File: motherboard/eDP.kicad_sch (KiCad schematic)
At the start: 4 parts, among them J2 20455-040E-76 OLED IPEX, J6 OLED EL POWER

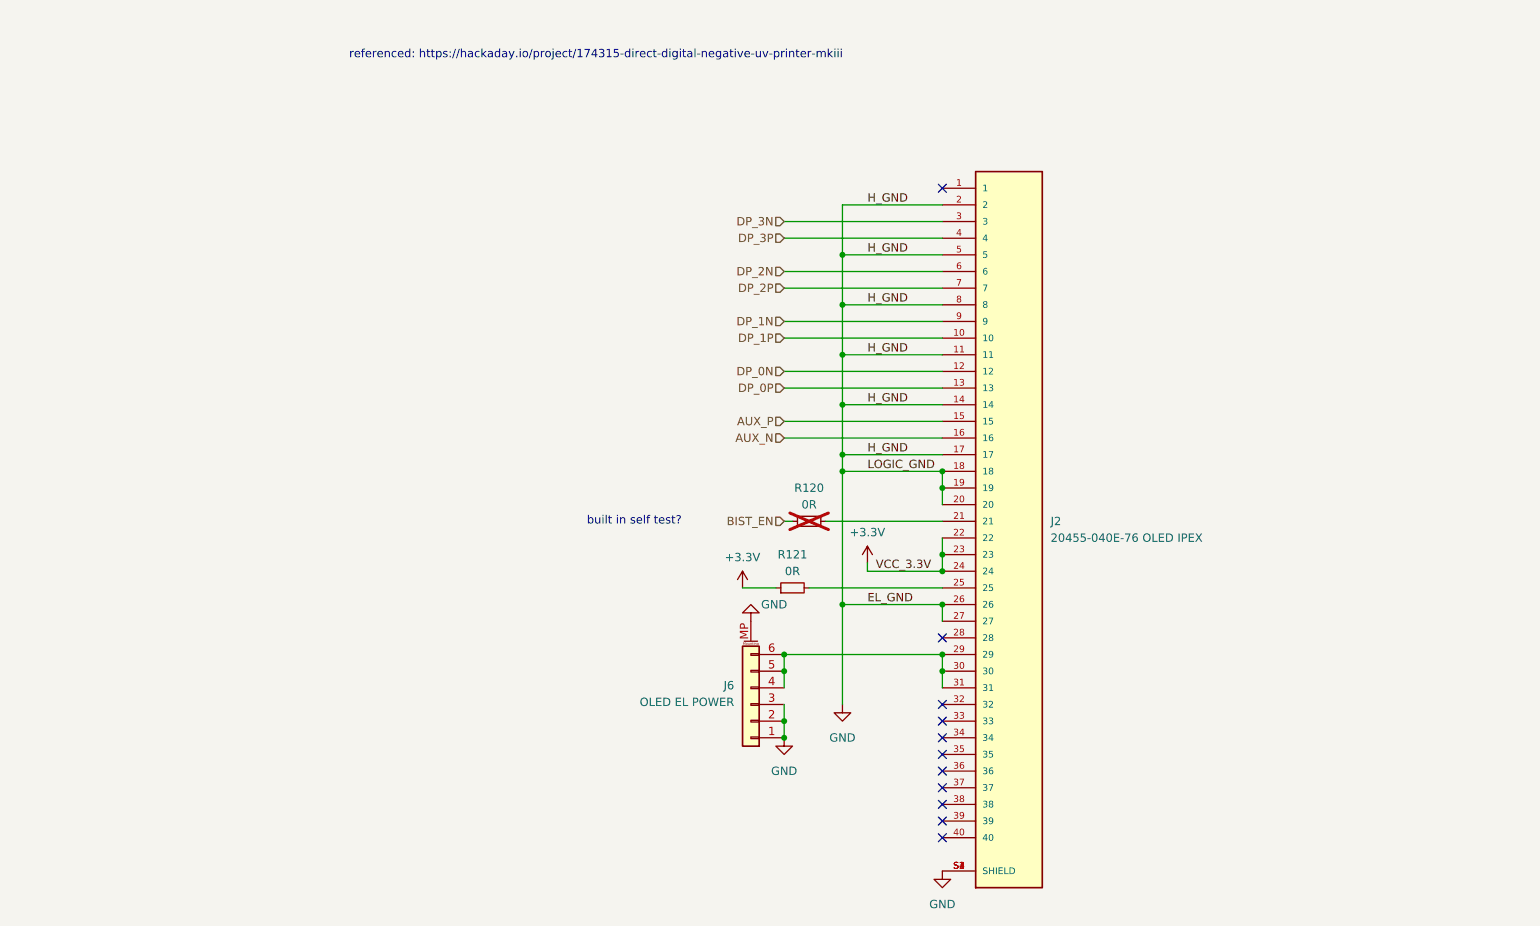
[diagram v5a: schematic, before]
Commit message: created display evaluation board + layout modifications
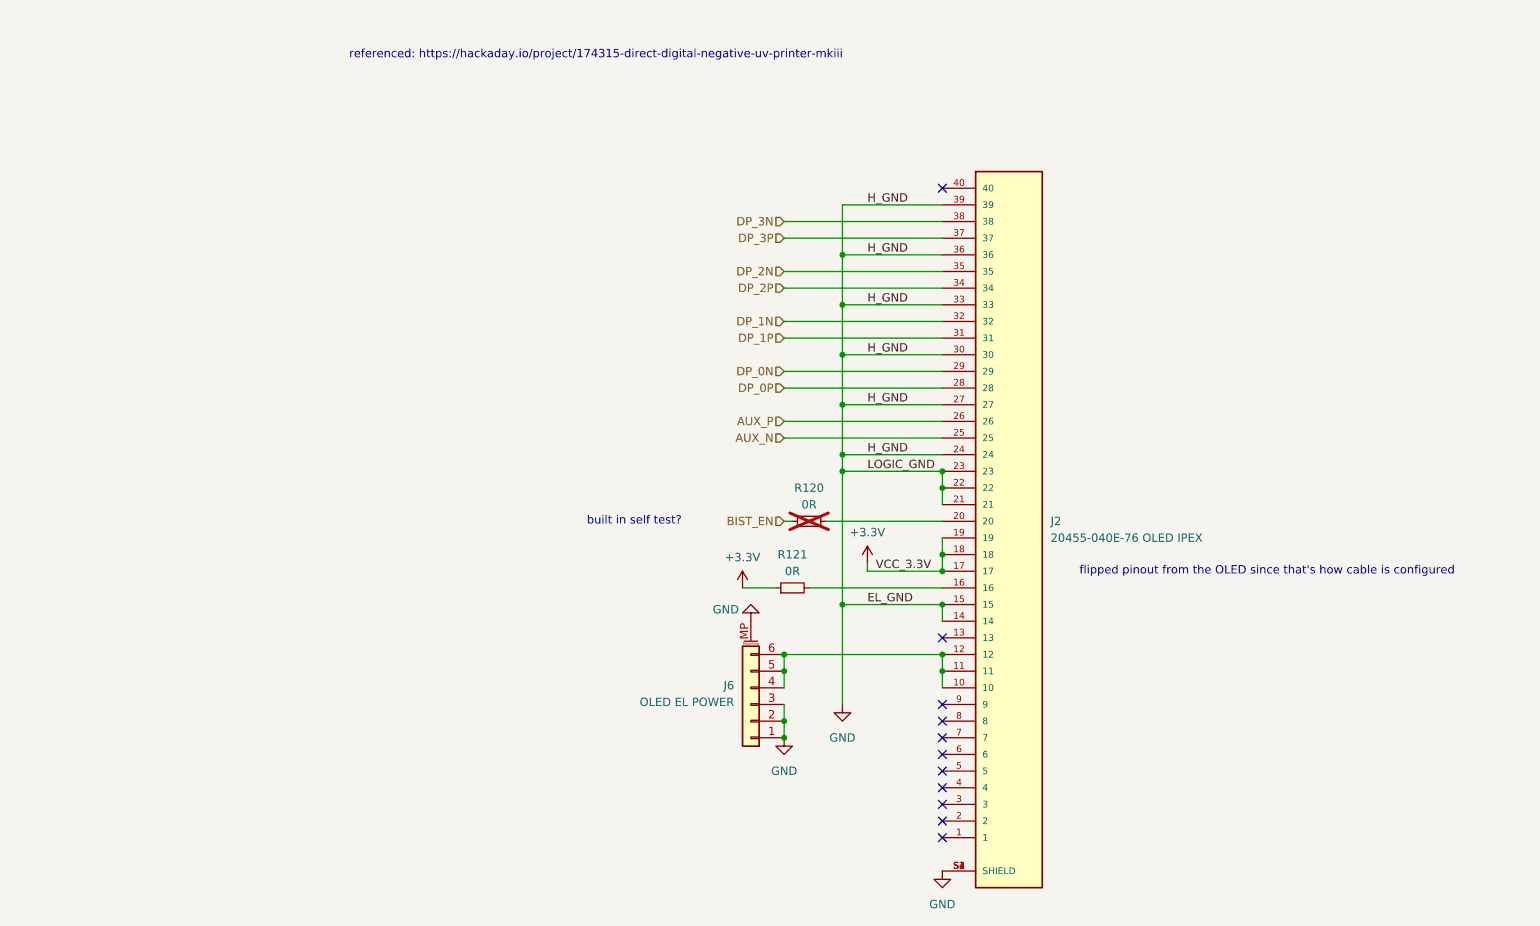
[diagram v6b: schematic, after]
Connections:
- net +3.3V: now also J2.17, J2.18, J2.19; no longer J2.22, J2.23, J2.24
- net AUX_N: now also J2.25; no longer J2.16
- net AUX_P: now also J2.26; no longer J2.15
- net DP_0N: now also J2.29; no longer J2.12
- net DP_0P: now also J2.28; no longer J2.13
- net DP_1N: now also J2.32; no longer J2.9
- net DP_1P: now also J2.31; no longer J2.10
- net DP_2N: now also J2.35; no longer J2.6
- net DP_2P: now also J2.34; no longer J2.7
- net DP_3N: now also J2.38; no longer J2.3
- net DP_3P: now also J2.37; no longer J2.4
- net GND: now also J2.15, J2.21, J2.22, J2.23, J2.24, J2.30, J2.33, J2.36, J2.39; no longer J2.11, J2.17, J2.18, J2.19, J2.2, J2.20, J2.26, J2.5, J2.8
- net at R121.2: now also J2.16; no longer J2.25
- net at R120.2: now also J2.20; no longer J2.21
- net at J6.4 (Pin_4), J6.5 (Pin_5), J6.6 (Pin_6): now also J2.10, J2.11, J2.12; no longer J2.29, J2.30, J2.31
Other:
- note added: "flipped pinout from the OLED since that's how cable is configured"
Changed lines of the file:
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@@
 		(comment 4 "Proof of concept board for feature verification")
+	)
+	(text "flipped pinout from the OLED since that's how cable is configured"
+		(exclude_from_sim no)
+		(at 203.2 107.95 0)
+		(effects
+			(font
+				(size 1.27 1.27)
+			)
+		)
 	)
 	(text "referenced: https://hackaday.io/project/174315-direct-digital-negative-uv-printer-mkiii"
@@
 			)
 			(justify right)
+		)
+	)
+	(symbol
+		(lib_id "power:GND")
+		(at 124.46 115.57 180)
+		(unit 1)
+		(exclude_from_sim no)
+		(in_bom yes)
+		(on_board yes)
+		(dnp no)
+		(property "Reference" "#PWR064"
+			(at 124.46 109.22 0)
+			(effects
+				(font
+					(size 1.27 1.27)
+				)
+				(hide yes)
+			)
+		)
+		(property "Value" "GND"
+			(at 120.65 113.792 0)
+			(effects
+				(font
+					(size 1.27 1.27)
+				)
+			)
+		)
+		(property "Footprint" ""
+			(at 124.46 115.57 0)
+			(effects
+				(font
+					(size 1.27 1.27)
+				)
+				(hide yes)
+			)
+		)
+		(property "Datasheet" ""
+			(at 124.46 115.57 0)
+			(effects
+				(font
+					(size 1.27 1.27)
+				)
+				(hide yes)
+			)
+		)
+		(property "Description" "Power symbol creates a global label with name \"GND\" , ground"
+			(at 124.46 115.57 0)
+			(effects
+				(font
+					(size 1.27 1.27)
+				)
+				(hide yes)
+			)
+		)
+		(pin "1"
+		)
+		(instances
+			(project "motherboard"
+				(path "/025fe4d1-0305-4b34-be04-f8d9818125a4/41516588-89d4-4c4a-8d7d-a4354a401e31"
+					(reference "#PWR064")
+					(unit 1)
+				)
+			)
 		)
 	)
@@
 					(unit 1)
 				)
-			)
-		)
-	)
-	(symbol
-		(lib_id "eDP_adaptor_board-rescue:GND-power")
-		(at 124.46 115.57 0)
-		(mirror x)
-		(unit 1)
-		(exclude_from_sim no)
-		(in_bom yes)
-		(on_board yes)
-		(dnp no)
-		(property "Reference" "#PWR0161"
-			(at 124.46 109.22 0)
-			(effects
-				(font
-					(size 1.27 1.27)
-				)
-				(hide yes)
-			)
-		)
-		(property "Value" "GND"
-			(at 128.016 113.03 0)
-			(effects
-				(font
-					(size 1.27 1.27)
-				)
-			)
-		)
-		(property "Footprint" ""
-			(at 124.46 115.57 0)
-			(effects
-				(font
-					(size 1.27 1.27)
-				)
-				(hide yes)
-			)
-		)
-		(property "Datasheet" ""
-			(at 124.46 115.57 0)
-			(effects
-				(font
-					(size 1.27 1.27)
-				)
-				(hide yes)
-			)
-		)
-		(property "Description" ""
-			(at 124.46 115.57 0)
-			(effects
-				(font
-					(size 1.27 1.27)
-				)
-			)
-		)
-		(pin "1"
-		)
-		(instances
-			(project "motherboard"
-				(path "/025fe4d1-0305-4b34-be04-f8d9818125a4/41516588-89d4-4c4a-8d7d-a4354a401e31"
-					(reference "#PWR0161")
-					(unit 1)
-				)

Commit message: starting motherboard v0.2
lessons from display eval v1
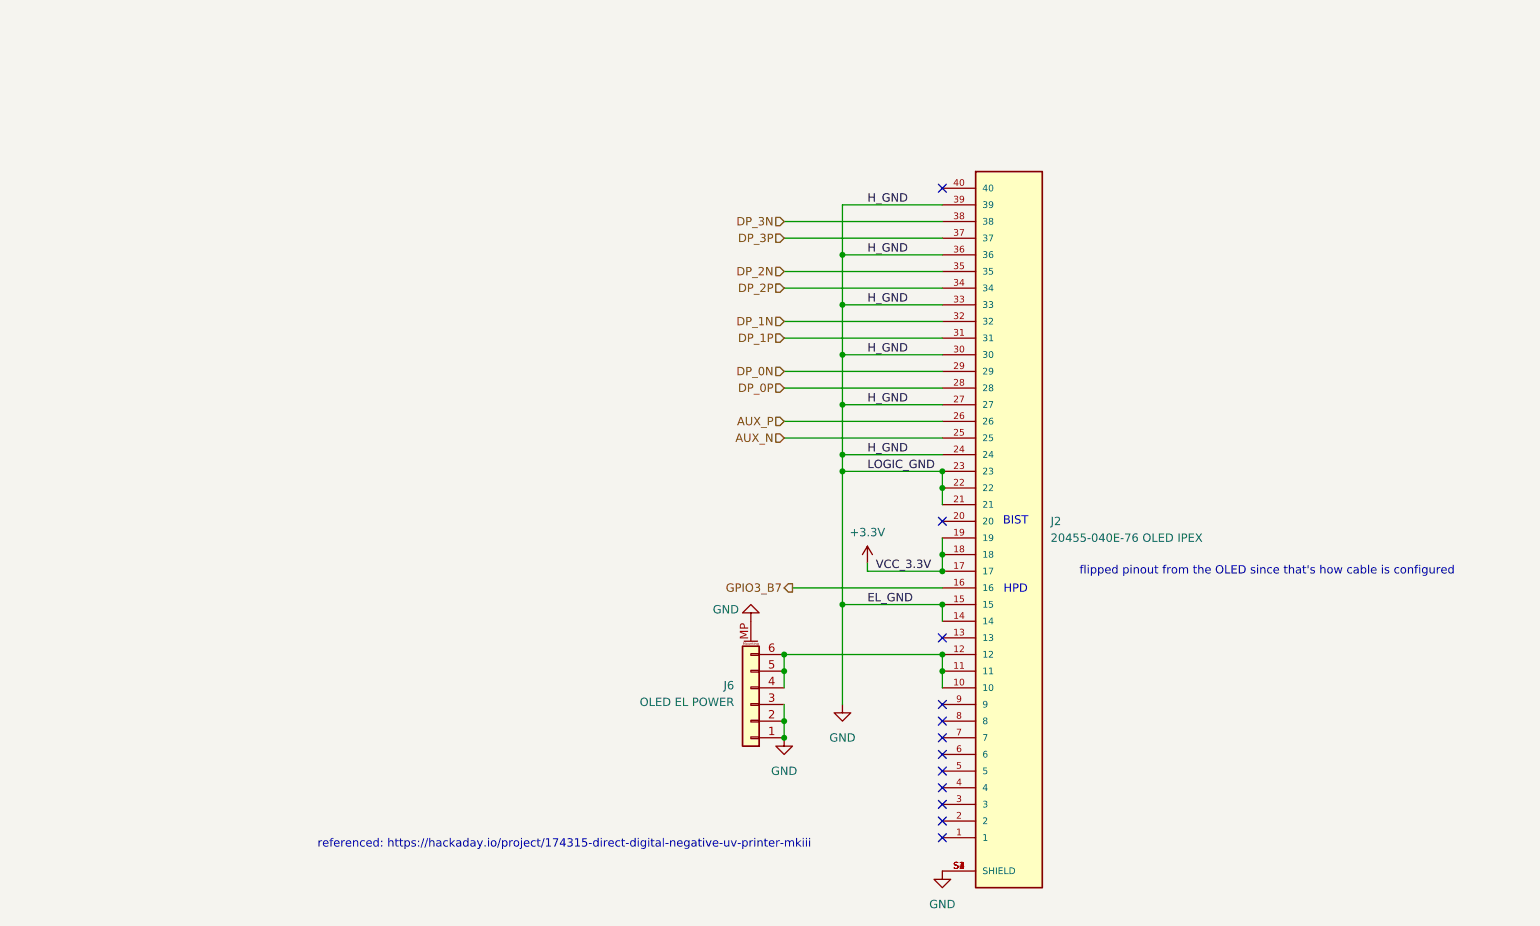
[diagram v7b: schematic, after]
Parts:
- removed R120, R121: 0R, Resistor_SMD:R_0402_1005Metric, symbol Device:R_Small
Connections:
- net GPIO3_B7: now reaches J2.16
- no-connect marks 11 -> 12
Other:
- note added: "BIST"
- note added: "HPD"
- note removed: "built in self test?"
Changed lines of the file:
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@@
+		)
+	)
+	(text "BIST"
+		(exclude_from_sim no)
+		(at 164.846 100.33 0)
+		(effects
+			(font
+				(size 1.27 1.27)
+			)
 		)
 	)
 	(text "referenced: https://hackaday.io/project/174315-direct-digital-negative-uv-printer-mkiii"
 		(exclude_from_sim no)
-		(at 100.838 29.21 0)
-		(effects
-			(font
-				(size 1.27 1.27)
-			)
-		)
-	)
-	(text "built in self test?"
+		(at 96.012 149.606 0)
+		(effects
+			(font
+				(size 1.27 1.27)
+			)
+		)
+	)
+	(text "HPD"
 		(exclude_from_sim no)
-		(at 106.68 100.33 0)
+		(at 164.846 110.744 0)
 		(effects
 			(font
@@
 	)
 	(no_connect
+		(at 153.67 100.33)
+	)
+	(no_connect
 		(at 153.67 140.97)
 	)
@@
 	(wire
 		(pts
-			(xy 133.35 110.49) (xy 153.67 110.49)
-		)
-		(stroke
-			(width 0)
-			(type default)
-		)
-	)
-	(wire
-		(pts
 			(xy 129.54 87.63) (xy 153.67 87.63)
 		)
@@
 	(wire
 		(pts
-			(xy 135.89 100.33) (xy 153.67 100.33)
-		)
-		(stroke
-			(width 0)
-			(type default)
-		)
-	)
-	(wire
-		(pts
 			(xy 138.43 74.93) (xy 153.67 74.93)
 		)
@@
 	(wire
 		(pts
-			(xy 129.54 100.33) (xy 130.81 100.33)
-		)
-		(stroke
-			(width 0)
-			(type default)
-		)
-	)
-	(wire
-		(pts
 			(xy 153.67 102.87) (xy 153.67 105.41)
 		)
@@
 	(wire
 		(pts
-			(xy 123.19 110.49) (xy 128.27 110.49)
+			(xy 130.81 110.49) (xy 153.67 110.49)
 		)
 		(stroke
@@
 		)
 	)
-	(hierarchical_label "BIST_EN"
-		(shape input)
-		(at 129.54 100.33 180)
-		(fields_autoplaced yes)
-		(effects
-			(font
-				(size 1.27 1.27)
-			)
-			(justify right)
-		)
-	)
 	(hierarchical_label "DP_2N"
 		(shape input)
@@
 		(shape input)
 		(at 129.54 64.77 180)
+		(fields_autoplaced yes)
+		(effects
+			(font
+				(size 1.27 1.27)
+			)
+			(justify right)
+		)
+	)
+	(hierarchical_label "GPIO3_B7"
+		(shape output)
+		(at 130.81 110.49 180)
 		(fields_autoplaced yes)
 		(effects
@@
 	)
 	(symbol
-		(lib_id "Device:R_Small")
-		(at 130.81 110.49 90)
-		(unit 1)
-		(exclude_from_sim no)
-		(in_bom yes)
-		(on_board yes)
-		(dnp no)
-		(fields_autoplaced yes)
-		(property "Reference" "R121"
-			(at 130.81 105.41 90)
-			(effects
-				(font
-					(size 1.27 1.27)
-				)
-			)
-		)
-		(property "Value" "0R"
-			(at 130.81 107.95 90)
-			(effects
-				(font
-					(size 1.27 1.27)
-				)
-			)
-		)
-		(property "Footprint" "Resistor_SMD:R_0402_1005Metric"
-			(at 130.81 110.49 0)
-			(effects
-				(font
-					(size 1.27 1.27)
-				)
-				(hide yes)
-			)
-		)
-		(property "Datasheet" "~"
-			(at 130.81 110.49 0)
-			(effects
-				(font
-					(size 1.27 1.27)
-				)
-				(hide yes)
-			)
-		)
-		(property "Description" "Resistor, small symbol"
-			(at 130.81 110.49 0)
-			(effects
-				(font
-					(size 1.27 1.27)
-				)
-				(hide yes)
-			)
-		)
-		(pin "1"
-		)
-		(pin "2"
-		)
-		(instances
-			(project "motherboard"
-				(path "/025fe4d1-0305-4b34-be04-f8d9818125a4/41516588-89d4-4c4a-8d7d-a4354a401e31"
-					(reference "R121")
-					(unit 1)
-				)
-			)
-		)
-	)
-	(symbol
 		(lib_id "power:GND")
 		(at 129.54 133.35 0)
@@
 				(path "/025fe4d1-0305-4b34-be04-f8d9818125a4/41516588-89d4-4c4a-8d7d-a4354a401e31"
 					(reference "#PWR0145")
-					(unit 1)
-				)
-			)
-		)
-	)
-	(symbol
-		(lib_id "Device:R_Small")
-		(at 133.35 100.33 90)
-		(unit 1)
-		(exclude_from_sim no)
-		(in_bom yes)
-		(on_board yes)
-		(dnp yes)
-		(fields_autoplaced yes)
-		(property "Reference" "R120"
-			(at 133.35 95.25 90)
-			(effects
-				(font
-					(size 1.27 1.27)
-				)
-			)
-		)
-		(property "Value" "0R"
-			(at 133.35 97.79 90)
-			(effects
-				(font
-					(size 1.27 1.27)
-				)
-			)
-		)
-		(property "Footprint" "Resistor_SMD:R_0402_1005Metric"
-			(at 133.35 100.33 0)
-			(effects
-				(font
-					(size 1.27 1.27)
-				)
-				(hide yes)
-			)
-		)
-		(property "Datasheet" "~"
-			(at 133.35 100.33 0)
-			(effects
-				(font
-					(size 1.27 1.27)
-				)
-				(hide yes)
-			)
-		)
-		(property "Description" "Resistor, small symbol"
-			(at 133.35 100.33 0)
-			(effects
-				(font
-					(size 1.27 1.27)
-				)
-				(hide yes)
-			)
-		)
-		(pin "1"
-		)
-		(pin "2"
-		)
-		(instances
-			(project "motherboard"
-				(path "/025fe4d1-0305-4b34-be04-f8d9818125a4/41516588-89d4-4c4a-8d7d-a4354a401e31"
-					(reference "R120")
 					(unit 1)
 				)
@@
 					(unit 1)
 				)
-			)
-		)
-	)
-	(symbol
-		(lib_id "power:+3.3V")
-		(at 123.19 110.49 0)
-		(unit 1)
-		(exclude_from_sim no)
-		(in_bom yes)
-		(on_board yes)
-		(dnp no)
-		(fields_autoplaced yes)
-		(property "Reference" "#PWR0144"
-			(at 123.19 114.3 0)
-			(effects
-				(font
-					(size 1.27 1.27)
-				)
-				(hide yes)
-			)
-		)
-		(property "Value" "+3.3V"
-			(at 123.19 105.8298 0)
-			(effects
-				(font
-					(size 1.27 1.27)
-				)
-			)
-		)
-		(property "Footprint" ""
-			(at 123.19 110.49 0)
-			(effects
-				(font
-					(size 1.27 1.27)
-				)
-				(hide yes)
-			)
-		)
-		(property "Datasheet" ""
-			(at 123.19 110.49 0)
-			(effects
-				(font
-					(size 1.27 1.27)
-				)
-				(hide yes)
-			)
-		)
-		(property "Description" "Power symbol creates a global label with name \"+3.3V\""
-			(at 123.19 110.49 0)
-			(effects
-				(font
-					(size 1.27 1.27)
-				)
-				(hide yes)
-			)
-		)
-		(pin "1"
-		)
-		(instances
-			(project "motherboard"
-				(path "/025fe4d1-0305-4b34-be04-f8d9818125a4/41516588-89d4-4c4a-8d7d-a4354a401e31"
-					(reference "#PWR0144")
-					(unit 1)
-				)

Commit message: v0.2 75 routes left!
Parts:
- J2: footprint eDP_Connector:IPEX_20455-040E-76 -> 20455-040E-76:IPEX_20455-040E-76
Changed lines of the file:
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@@
 			)
 		)
-		(property "Footprint" "eDP_Connector:IPEX_20455-040E-76"
+		(property "Footprint" "20455-040E-76:IPEX_20455-040E-76"
 			(at 163.83 100.33 0)
 			(effects
